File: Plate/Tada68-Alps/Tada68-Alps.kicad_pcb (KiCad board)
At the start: 2 copper layers, 304.8 x 95.3 mm, 1 part

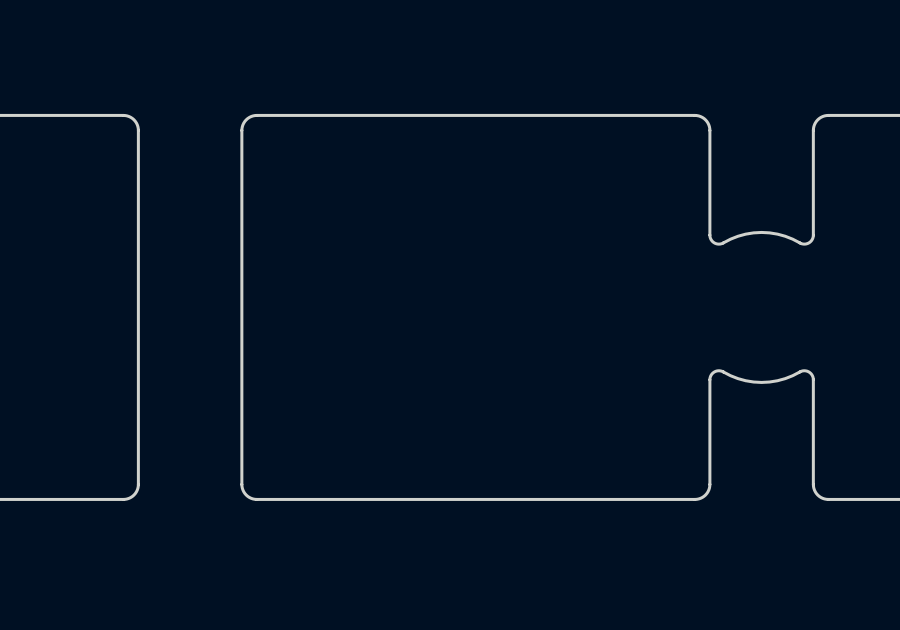
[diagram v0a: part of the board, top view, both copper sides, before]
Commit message: Create plate files with dummy drill files
Because fab complains
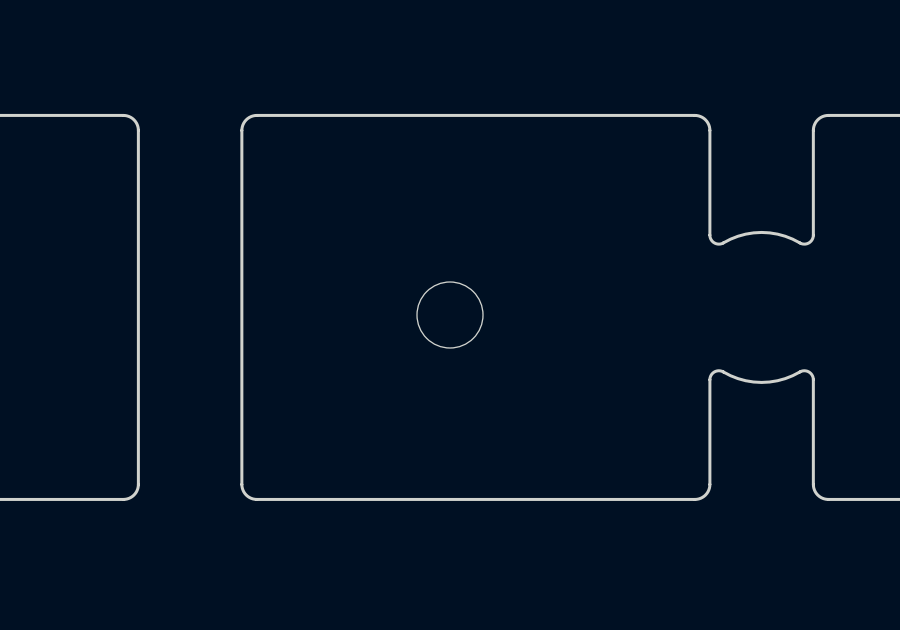
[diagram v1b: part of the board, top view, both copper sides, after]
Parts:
- added REF**: MountingHole_2.2mm_M2, Mounting_Holes:MountingHole_2.2mm_M2, F.Cu at (137.3, 66.7)
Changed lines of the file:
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@@
 (kicad_pcb (version 4) (host pcbnew 4.0.7)
   (general
-    (links 1)
+    (links 0)
     (no_connects 1)
     (area 15.875 15.875 333.375001 119.062501)
@@
     (tracks 0)
     (zones 0)
-    (modules 1)
+    (modules 2)
     (nets 2)
   )
@@
     (pad_to_mask_clearance 0.2)
     (aux_axis_origin 0 0)
-    (visible_elements FFFFFF7F)
+    (visible_elements 7FFFFFFF)
     (pcbplotparams
       (layerselection 0x010f0_80000001)
@@
       (net 1 GND))
   )
+  (module Mounting_Holes:MountingHole_2.2mm_M2 (layer F.Cu)
+    (at 137.287 66.675)
+    (descr "Mounting Hole 2.2mm, no annular, M2")
+    (tags "mounting hole 2.2mm no annular m2")
+    (attr virtual)
+    (fp_text reference REF** (at 0 -3.2) (layer Dwgs.User)
+      (effects (font (size 1 1) (thickness 0.15)))
+    )
+    (fp_text value MountingHole_2.2mm_M2 (at 0 3.2) (layer F.Fab)
+      (effects (font (size 1 1) (thickness 0.15)))
+    )
+    (fp_text user %R (at 0.3 0) (layer F.Fab)
+      (effects (font (size 1 1) (thickness 0.15)))
+    )
+    (fp_circle (center 0 0) (end 2.2 0) (layer Cmts.User) (width 0.15))
+    (fp_circle (center 0 0) (end 2.45 0) (layer F.CrtYd) (width 0.05))
+    (pad 1 np_thru_hole circle (at 0 0) (size 2.2 2.2) (drill 2.2) (layers *.Cu *.Mask))
+  )
   (gr_text "65\n" (at 200.533 103.505) (layer F.Mask)
